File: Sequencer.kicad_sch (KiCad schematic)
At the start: 49 parts, among them J1 Screw_Terminal_01x12, J3 USB_C_Receptacle_USB2.0_16P, SW1 Switch, U1 ATtiny814-SS, U2 TLP3123, U3 TLP3123, U4 TLP3123, U5 TLP3123, U6 MC78L05_SOT89, U7 FT230XS

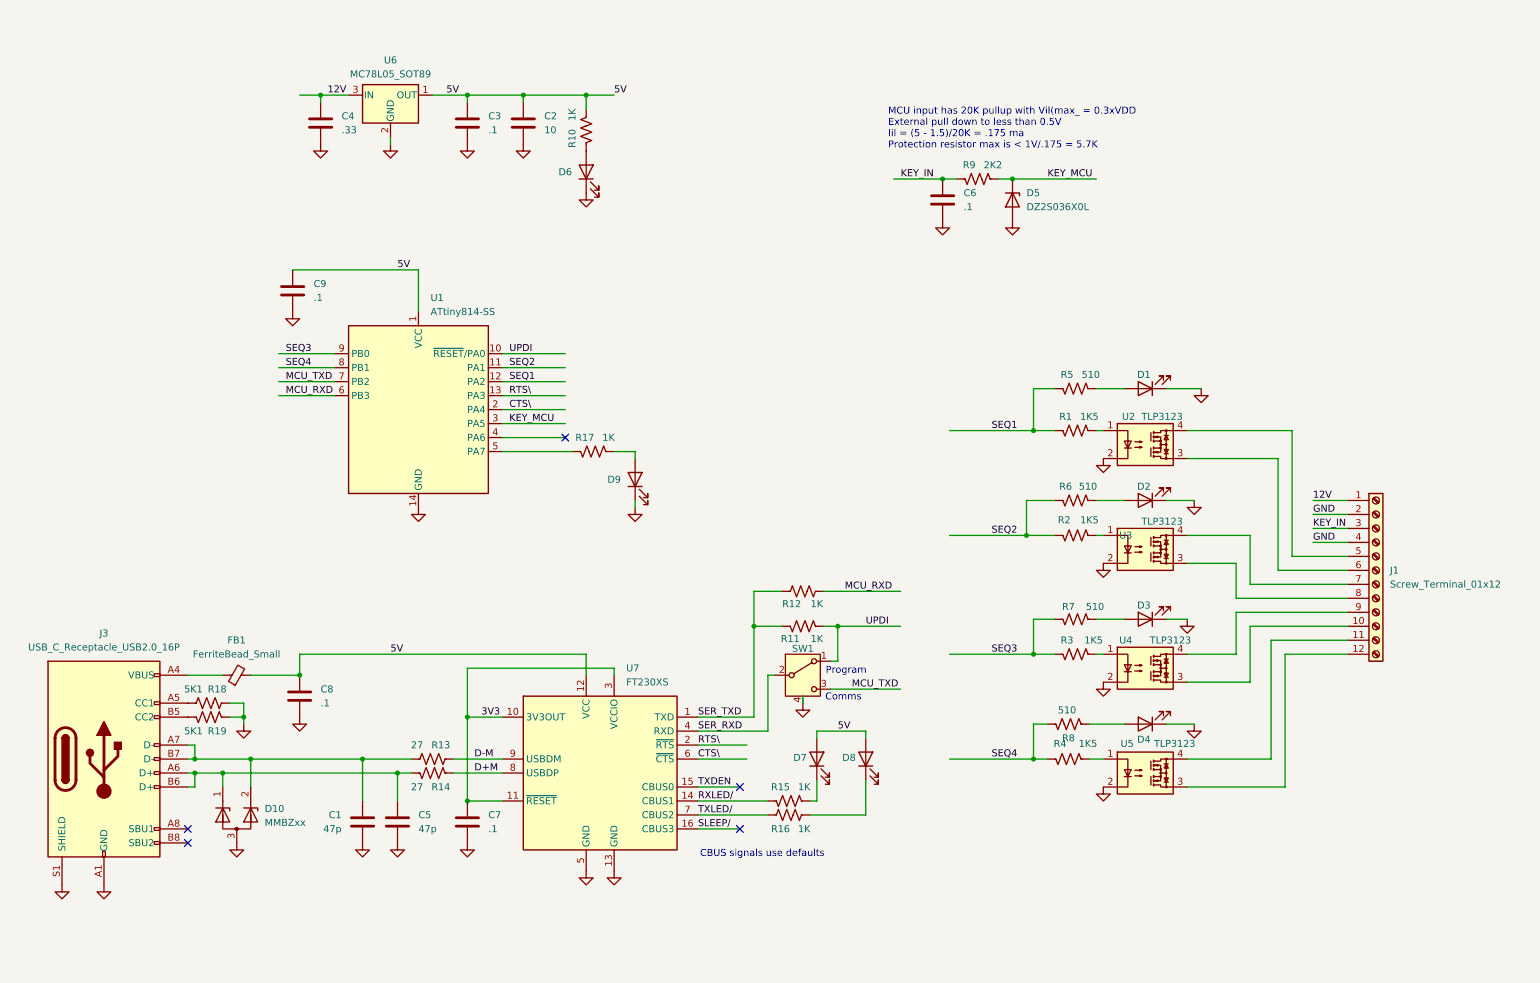
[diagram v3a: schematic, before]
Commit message: Added optocoupler on KEY line Changed to ATTinyx16 processor with 20 pins Serial select for UPDI vs Serial comms is now a pin header Added pin header for other unused signals on MCU
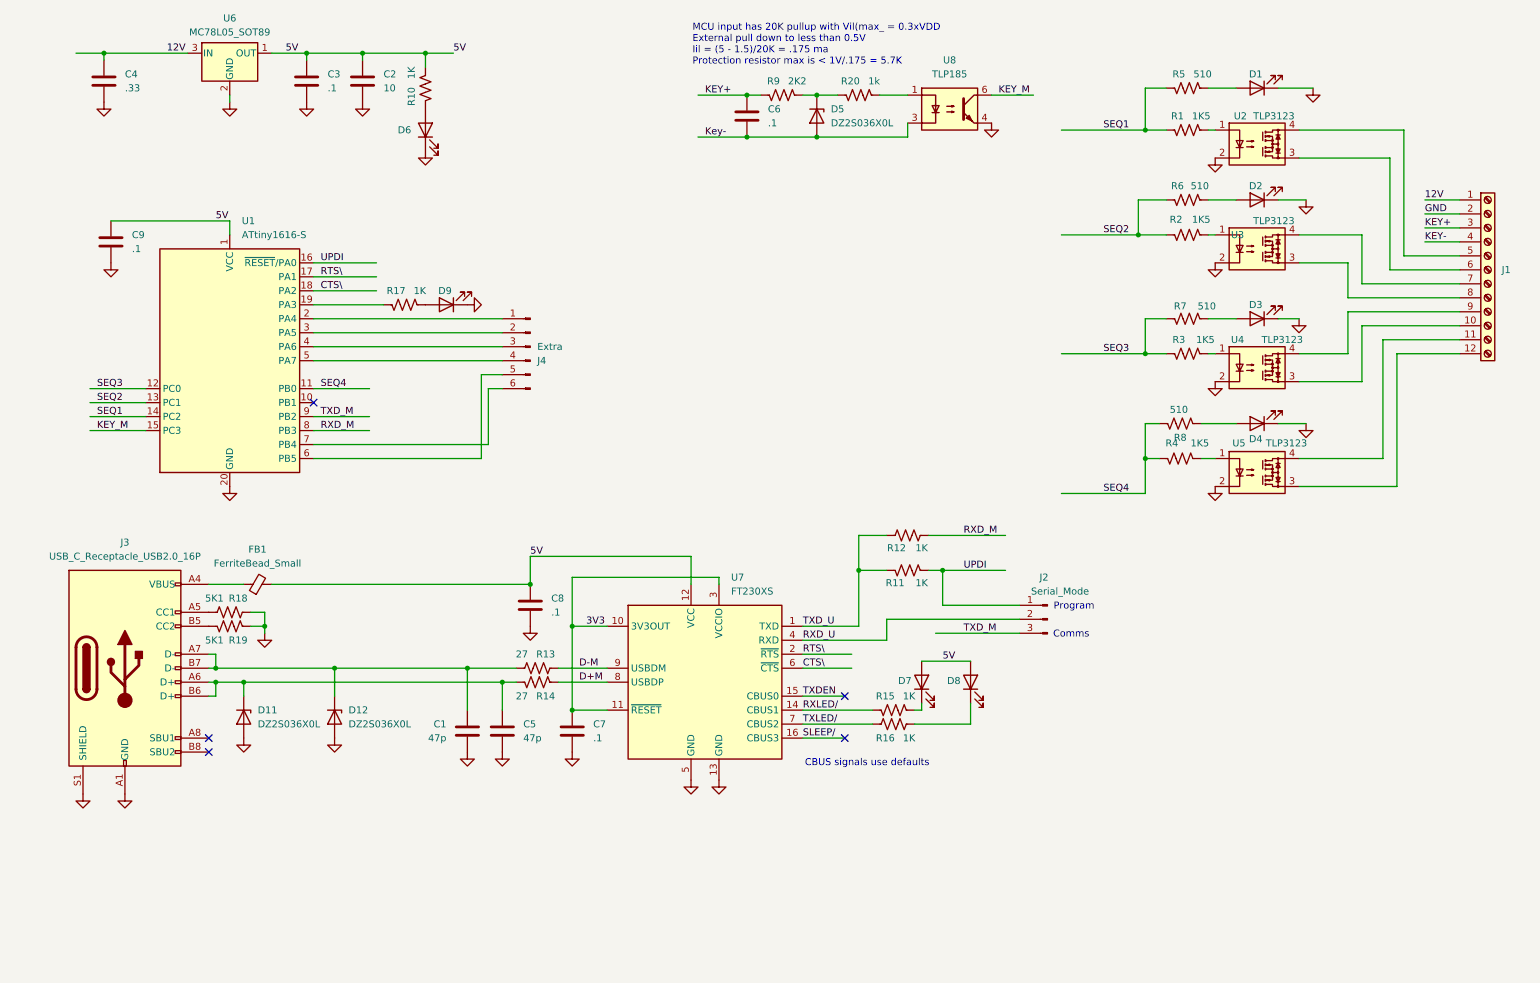
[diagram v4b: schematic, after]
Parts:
- removed D10: MMBZxx, Package_TO_SOT_SMD:SOT-23, symbol Diode:MMBZxx
- removed SW1: Switch, Library:SLW-1277744-3a-n-d, symbol Switch:SW_SPDT
- removed U1: ATtiny814-SS, Package_SO:SOIC-14_3.9x8.7mm_P1.27mm, symbol MCU_Microchip_ATtiny:ATtiny814-SS
- added D11, D12: DZ2S036X0L, Diode_SMD:D_SOD-523, symbol Diode:DZ2S036X0L
- added J2: Serial_Mode, Connector_PinHeader_2.54mm:PinHeader_1x03_P2.54mm_Vertical, symbol Connector:Conn_01x03_Pin
- added J4: Extra, Connector_PinHeader_2.54mm:PinHeader_1x06_P2.54mm_Vertical, symbol Connector:Conn_01x06_Pin
- added R20: 1k, Resistor_SMD:R_0603_1608Metric, symbol Device:R_US
- added U1: ATtiny1616-S, Package_SO:SOIC-20W_7.5x12.8mm_P1.27mm, symbol MCU_Microchip_ATtiny:ATtiny1616-S
- added U8: TLP185, Package_SO:SOIC-4_4.55x3.7mm_P2.54mm, symbol Isolator:TLP185
- R11, R12: footprint Resistor_SMD:R_0805_2012Metric -> Resistor_SMD:R_0603_1608Metric
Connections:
- net 5V: now also U1.1 (VCC)
- net CTS\: now also U1.18 (PA2)
- net GND: now also D11.2 (A), D12.2 (A), U1.20 (GND), U8.4; no longer C6.2, D5.2 (A), J1.4 (Pin_4)
- net RTS\: now also U1.17 (PA1)
- net SEQ1: now also U1.14 (PC2)
- net SEQ2: now also U1.13 (PC1)
- net SEQ3: now also U1.12 (PC0)
- net SEQ4: now also U1.11 (PB0)
- net UPDI: now also J2.1 (Pin_1), U1.16 (~{RESET}/PA0)
- net at R17.1: now also U1.19 (PA3)
- net at C1.1, J3.A7 (D-), J3.B7 (D-)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: now also D12.1 (K)
- net at C5.1, J3.A6 (D+), J3.B6 (D+)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: now also D11.1 (K)
- net KEY_IN renamed KEY+
- net KEY_MCU: no longer names the net of D5.1 (K), R9.2
- net KEY_MCU: now also R20.1
- net MCU_RXD renamed RXD_M
- net RXD_M: now also U1.8 (PB3)
- net SER_RXD renamed RXD_U
- net RXD_U: now also J2.2 (Pin_2)
- net SER_TXD renamed TXD_U
- new net: J4.1 (Pin_1), U1.2 (PA4)
- new net: J4.2 (Pin_2), U1.3 (PA5)
- new net: J4.3 (Pin_3), U1.4 (PA6)
- new net: J4.4 (Pin_4), U1.5 (PA7)
- new net: J4.5 (Pin_5), U1.6 (PB5)
- new net: J4.6 (Pin_6), U1.7 (PB4)
- new net: R20.2, U8.1
- new net KEY-: J1.4 (Pin_4)
- new net KEY_M: U1.15 (PC3), U8.6
- new net Key-: C6.2, D5.2 (A), U8.3
- new net TXD_M: J2.3 (Pin_3), U1.9 (PB2)
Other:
- moved on the sheet: C1, C2, C3, C4, C5, C6, C7, C8, C9, D1, D2, D3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
